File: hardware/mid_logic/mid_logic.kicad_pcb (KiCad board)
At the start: 4 copper layers, 52 x 52 mm, 49 parts, among them J2 J_STK_A, J3 J_STK_B, J7 USB-C, Q2 BC847, SW1 RESET, SW2 BOOT, U1 ESP32-S3-WROOM-1-N16R8, U2 MAX3485, U3 PCF8575, U4 PhotoMOS 60V, U5 USBLC6-2SC6

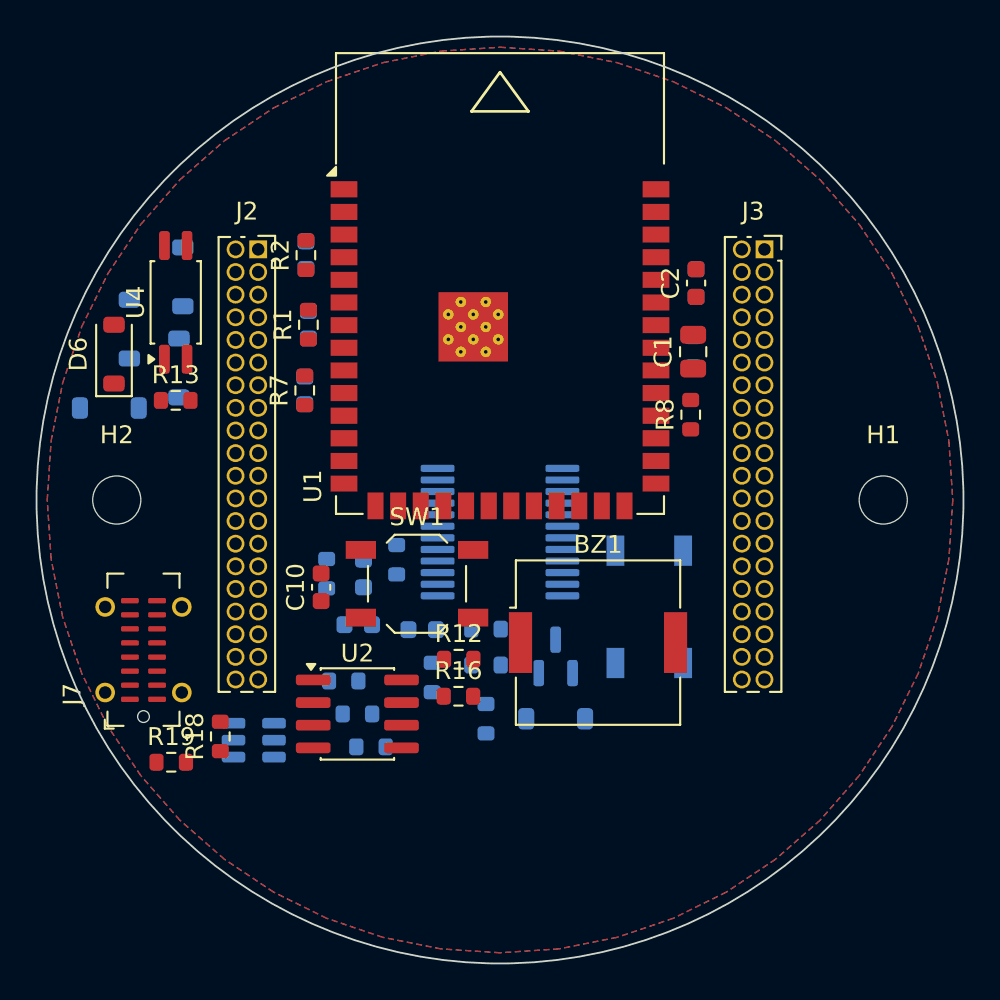
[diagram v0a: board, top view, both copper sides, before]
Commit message: Alle drei Boards kupferfehlerfrei, und die Bilder zeigen endlich die Stecker
ROUTING. Alle drei Platinen haben jetzt null Kupferfehler:

  Top     179 Segmente,  22 Vias,  7 Signale offen  (vorher 11, 2 Fehler)
  Mid     720 Segmente,  74 Vias,  4 Signale offen  (vorher  6)
  Bottom  811 Segmente,  91 Vias,  6 Signale offen  (vorher  8, 6 Fehler)

Top hatte zwei copper_edge_clearance-Fehler an der USB-C-Kerbe: Eine
BTN2-Bahn lief auf In1.Cu quer durch den Ausschnitt. Der Randkeepout des
Routers kannte die Kerbe gar nicht - er bestand aus vier Balken entlang der
Kanten, und die Kerbe schneidet in eine dieser Kanten hinein. Die einzige
Aussparung darin stammte noch von der Klinkenbuchse, die es nicht mehr gibt.
route_boards.py setzt jetzt NOTCH_KEEPOUT.

M1_ISNS AUF BOTTOM IST MIT ABSICHT LEER. Freerouting hatte das analoge
Motorstrom-Messsignal auf F.Cu direkt an die Vergleichsschwelle V_TRIP_LO
gepresst - vier Kurzschluesse, eine Kreuzung, ein Abstandsfehler, alle in
einem Feld von zwei Millimetern. Einzeln herausgeloeste Segmente haben das
Problem nur verschoben: nach jedem Eingriff dieselben zwei Netze an der
naechsten Stelle. Das Netz ist deshalb komplett entfernt und wird von Hand
gezogen. Sachlich ist die Paarung ohnehin die schlechteste denkbare - koppeln
Messsignal und Ausloeseschwelle, verstimmt sich die Hinderniserkennung
selbst, ohne dass eine DRC das je bemerkt. docs/16 erklaert es samt Auflagen.

DIE BILDER ZEIGTEN DIE STECKVERBINDER NICHT - und es lag nicht an den
Modellen. Die Bildkette war nie ein Skript, sondern jedes Mal von Hand
getippt. Dadurch stammten die Teile aus verschiedenen Zeitpunkten: Modelle
16:04, Stapel-STEPs 15:59, Unterseiten-Renderings 13:41. Ausgerechnet die
Unterseiten zeigen den Feldstecker und die USB-Buchse.

tools/render_all.py macht daraus einen Aufruf: sechs Boardansichten, drei
STEP-Ausgaben mit Modellen, das Stapelbild und die Gesamtbaugruppe - ein
Zeitstand fuer alles. Renderings jetzt mit transparentem Hintergrund, damit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
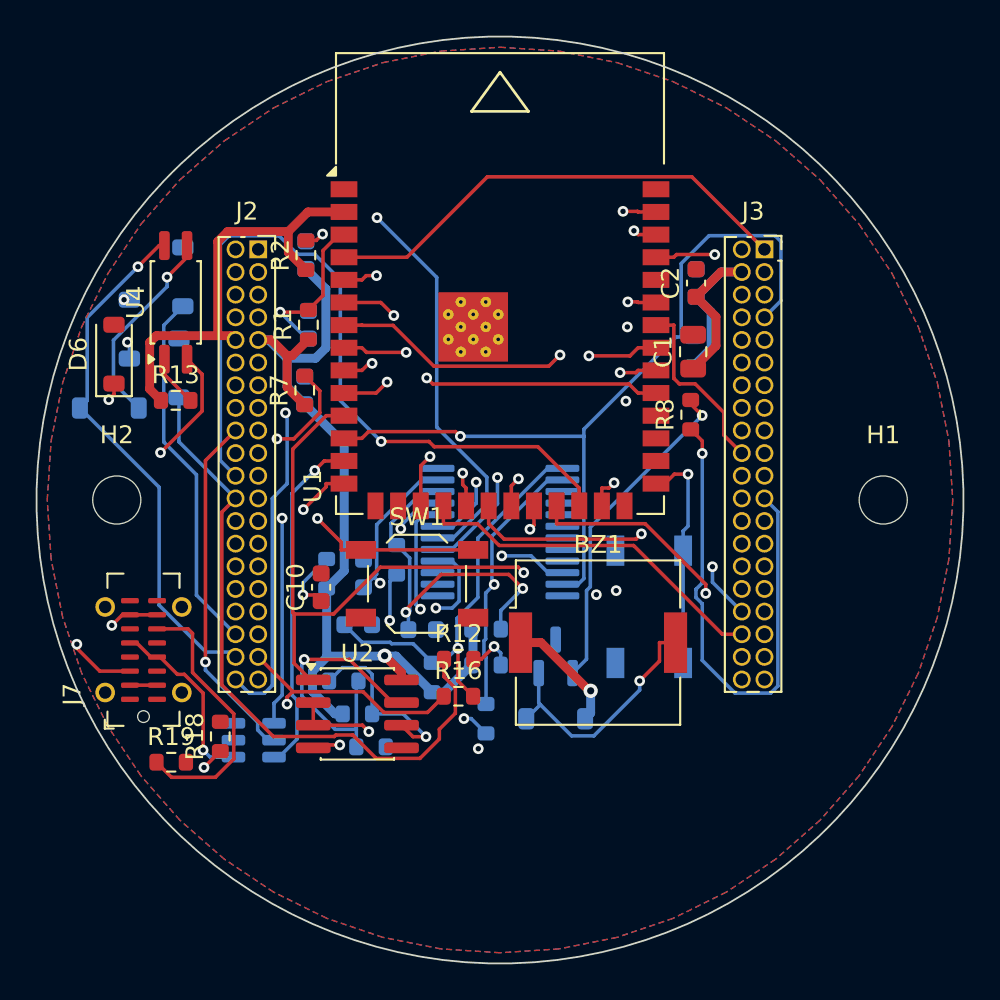
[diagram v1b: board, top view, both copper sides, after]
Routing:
- net 3V3_SYS: track 0.00 -> 124.0 mm, vias 0 -> 1
- net I2C_SCL: track 0.00 -> 61.6 mm, vias 0 -> 4
- net AUDIO_PWM: track 0.00 -> 56.9 mm, vias 0 -> 3
- net UART485_TX: track 0.00 -> 54.0 mm, vias 0 -> 2
- net TRIP_RST: track 0.00 -> 52.5 mm, vias 0 -> 1
- net SAB2_IN: track 0.00 -> 49.6 mm, vias 0 -> 2
- net HW_TRIP1: track 0.00 -> 49.0 mm, vias 0 -> 2
- net UART485_RX: track 0.00 -> 48.3 mm, vias 0 -> 1
- net I2C_SDA: track 0.00 -> 46.8 mm, vias 0 -> 1
- net I_SENSE2: track 0.00 -> 44.7 mm, vias 0 -> 1
- net M2_INB: track 0.00 -> 44.5 mm, vias 0 -> 1
- net SAB1_IN: track 0.00 -> 44.4 mm, vias 0 -> 2
- net PRESENCE_INT: track 0.00 -> 43.6 mm, vias 0 -> 1
- net 5V_SYS: track 0.00 -> 42.3 mm, vias 0 -> 1
- net RELAY_CTL: track 0.00 -> 42.0 mm, vias 0 -> 2
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
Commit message: Hauptschalter, Magnetkontakt im Rahmen, verschraubter Stapel - Umbau v0.7
VIER ENTSCHEIDUNGEN VOM 19.08.2026, alle umgesetzt:

1. HAUPTSCHALTER. Bisher stand nach dem Verschrauben von Bottom und Mid
sofort 24 V auf allem - ohne dass das Top-Board steckte. Jetzt laeuft der
Gate-Pulldown des Verpolschutz-FETs als SCHLEIFE durch den Stapel:
Q1-Gate -> R1 -> EN_LOOP (Stapelkontakt B2, war PGND; Pinout v0.7) -> SW5
auf Top -> PGND. Neuer 1-M-Pullup R1B haelt das Gate bei offener Schleife
definiert an der Source. Top-Board fehlt ODER SW5 aus -> Q1 sperrt, nichts
bekommt 24 V. Der Schalter traegt nur den Teilerstrom (~20 uA).
SW5 ist ein Copal CVS-01 (1,5 mm hoch, unter der Scheibe, durch eine
Oeffnung bedienbar). Er sitzt HOCHKANT bei (11,9/-19,4): Das Fenster
zwischen ToF-Courtyard (bis 8,245) und Ecktaster (ab 15,205) ist 6,96 mm
breit, der Schalter waagerecht 7,69 - drei Anlaeufe bei 12,5, 11,0 und 11,9
endeten in DRC-Ueberlappungen, erst das Ausmessen statt Schaetzens der
Courtyards zeigte, dass NUR gedreht Platz ist.

2. MAGNETKONTAKT IN DEN ABDECKRAHMEN, unten mittig - dort haelt auch das
vorhandene DCX-909 (Gewinde OD 8, im Rahmen ist Platz; Messpunkt F14: ist
der Rahmen dort hohl?). Das Magnetlangloch im Top-Board (Zwischenloesung
von einem Tag) ist wieder raus, mit ihm die 6,8-mm-Grenze, an der jedes
Kaufteil scheiterte. Neu: KABELKERBE 5 x 2 unten mittig, J6 dahinter
mittig auf der Rueckseite. Router-Keepout entsprechend getauscht.

3. LOETSCHEIBE hardware/stern_puck/ (OE 16, zweilagig, DRC null Fehler):
verbindet die Steckseite des DCX-909 mit den Litzen des Sterns. Litzen
durch Fesselbohrungen faedeln, umschlagen, loeten - die Zugentlastung ist
die Bohrung, nicht das Zinn. Drei eigene DRC-Runden gebraucht: 2,0er Pads
beruehren sich bei 1,85 Stiftabstand, die Minus-Bruecke lief durch das
Plus-Pad, die Fesselbohrungen brauchten seitliche Lage und OE 16 statt 14.

4. BEFESTIGUNGSKONZEPT v2 (docs/04, 2b): verschraubt statt nur gesteckt.
NEU mechanical/tragring.py 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
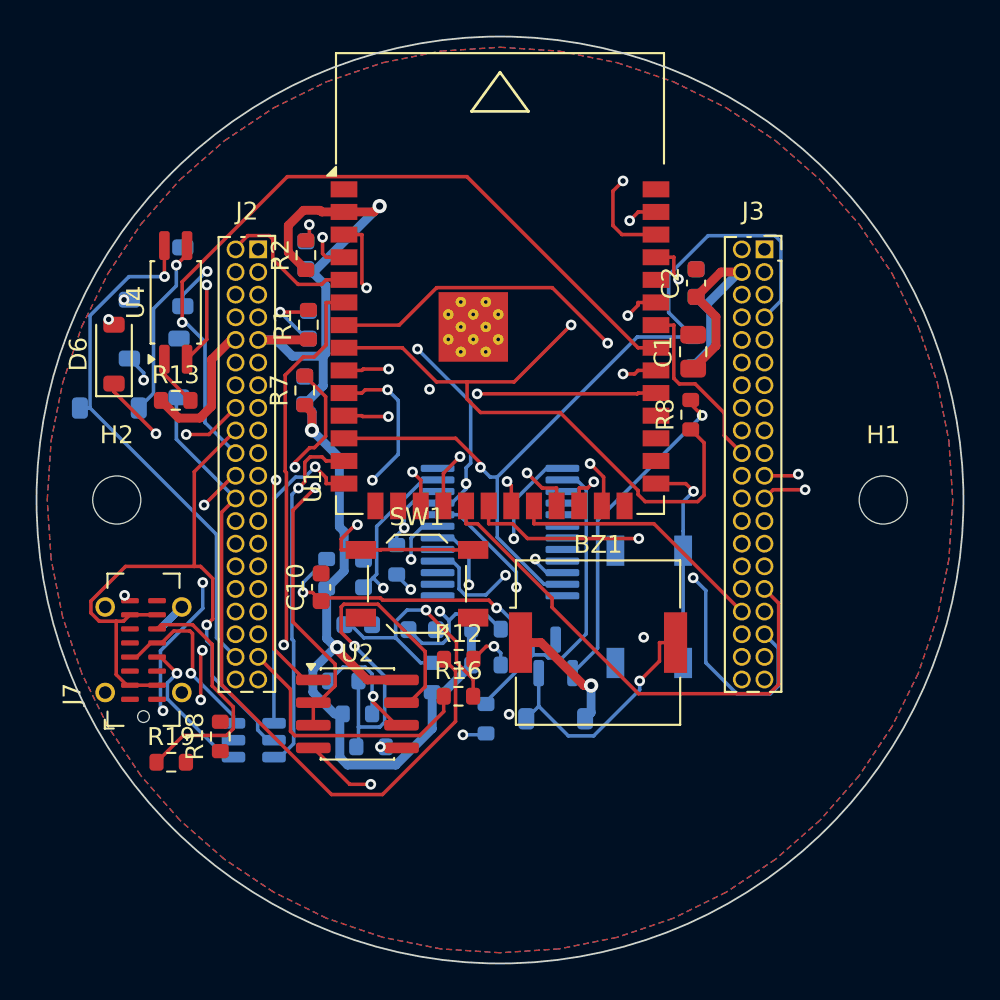
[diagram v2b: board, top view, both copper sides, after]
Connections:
- J3 pad 2: PGND -> EN_LOOP
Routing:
- net TRIP_RST: track 52.5 -> 29.1 mm
- net HW_TRIP2: track 21.9 -> 0.00 mm, vias 1 -> 0
- net USB_CC1: track 15.4 -> 0.00 mm, vias 2 -> 0
- net RS485_DIR: track 37.0 -> 49.6 mm
- net M2_INB: track 44.5 -> 54.9 mm, vias 1 -> 3
- net USB_DP_C: track 0.00 -> 10.2 mm, vias 0 -> 1
- net AUDIO_PWM: track 56.9 -> 66.9 mm, vias 3 -> 2
- net M1_INA: track 38.4 -> 47.8 mm, vias 1 -> 2
- net RS485_B: track 19.3 -> 28.1 mm
- net USB_VBUS: track 30.3 -> 37.7 mm, vias 2 -> 1
- net RELAY_CTL: track 42.0 -> 48.5 mm, vias 2 -> 3
- net PGND: track 0.00 -> 6.00 mm, vias 1 -> 4
- net I2C_SCL: track 61.6 -> 66.9 mm, vias 4 -> 3
- net HW_TRIP1: track 49.0 -> 43.9 mm, vias 2 -> 4
- net RS485_A: track 28.8 -> 23.8 mm, vias 1 -> 3
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
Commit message: Leistungsvias, Via-Strompruefung, Reset/Boot-Durchgriffe und der Gehaeusebecher
VIER ARBEITEN AUS EINEM ABEND, alle aus Rueckfragen entstanden:

1. VIAS SIND NICHT BELIEBIG STROMTRAGFAEHIG - der Einwand traf: 24V_IN
lief ueber genau EIN 0,6/0,3-Via (~1,2 A) bei 4,1 A Grenzstrom, dazu 14
weitere Engpaesse auf Bottom. Ursache: Die Bottom-Klassen routeten mit dem
Standardvia - ein Erbe der diskreten H-Bruecke, zwischen deren FETs das
0,8er nicht passte; Mid und Top hatten das Leistungsvia laengst. Jetzt:
PWR- und RAIL-Klasse auf Bottom mit 0,8/0,4, Massebruecken dort ebenso
(deren Platzsuche folgt jetzt der Viagroesse - die alte 0,6er-Suche setzte
0,8er-Vias in 0,6er-Luecken, vier Abstandsfehler).

NEU tools/via_check.py: prueft nach jedem Routing jedes Via gegen den
Dauerstrom seines Netzes (4 A je mm Bohrung, 3-mm-Parallelgruppen);
--fix setzt Zwillingsvias. Zwei eigene Fehler auf dem Weg, beide vom
Werkzeug selbst aufgedeckt: KiCad-10-Formabfragen brauchen eine Lage, und
die erste Freiraumpruefung sah nur F/B - ein Via bohrt aber durch ALLE
vier Lagen; 15 Innenlagen-Kurzschluesse, alle rueckstandslos entfernt.
Endstand: 27 Zwillinge gesetzt, 11 dokumentierte Engpaesse als
Handarbeitsliste mit Koordinaten in docs/16.

2. RESET UND BOOT WAREN UNERREICHBAR - SW1 sass mitten unter dem
Top-Board, SW2 zeigte zur Rueckseite. Beide jetzt auf Mids Vorderseite bei
(+-8/18,6), darueber zwei OE-3,2-Durchgriffe H3/H4 im Top-Board: Scheibe
ab, Stift durch, druecken. Im Betrieb verdeckt die Scheibe die Loecher.

3. DER GEHAEUSEBECHER (mechanical/gehaeuse.py): kapselt Bottom und Mid,
Rueckwand mit Tunnelfenster fuer die Feldstecker-Leiste - sie bleibt als
einziges von hinten zugaenglich. Verbindung zum Tragring per BAJONETT:
drei Zapfen an 12/3/9 Uhr, ~7 Grad Drehung, tangential auskragende
Koepfe - radiale Rasthaken scheiterten dreifach (Adapter auf den
Diagonalen, Dosenwand aussen, Adapterbasis innen; frei ist nur ein
2,2-mm-Band auf den Achsen). Wand an den Schraubdomen gefenste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
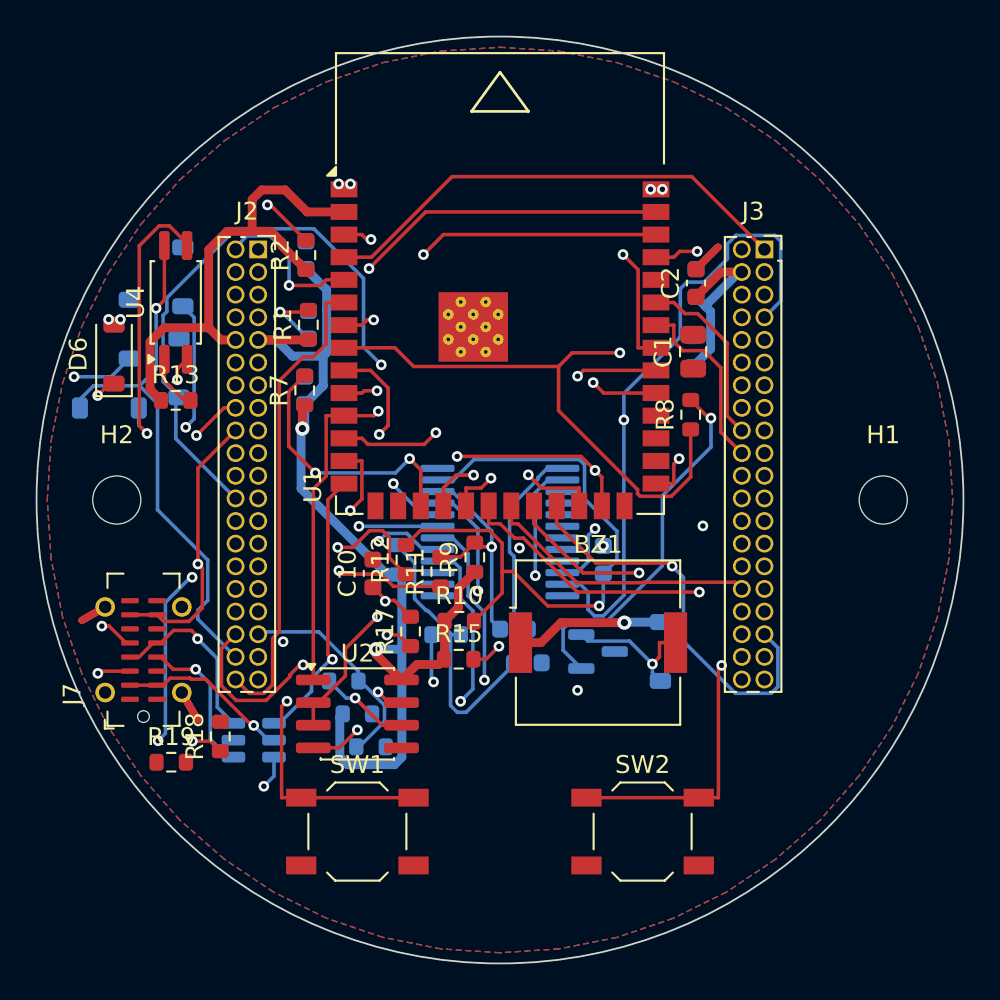
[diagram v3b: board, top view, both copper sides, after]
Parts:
- R10, R11, R15, R17, R9, SW2: moved to F.Cu
- R16: moved to B.Cu
- moved SW1 14.3 mm to (-8.00, 18.6)
- moved C8 13.5 mm to (5.80, 3.35)
- moved SW2 12.6 mm to (8.00, 18.6), turned to 0 degrees
- moved C9 9.75 mm to (1.56, 9.14)
- moved R15 8.82 mm to (-2.32, 8.93), turned to 0 degrees
- moved D1 6.98 mm to (9.00, 8.50), turned to 90 degrees
- moved R14 6.90 mm to (-5.80, 3.35)
- moved R17 6.47 mm to (-5.02, 7.37)
- moved R12 6.32 mm to (-5.28, 3.35), turned to 90 degrees
- moved C7 5.15 mm to (0.78, 7.24)
- moved R9 4.08 mm to (-1.41, 3.21), turned to 90 degrees
- moved R16 3.52 mm to (-3.02, 7.56)
- moved C10 3.00 mm to (-7.13, 4.12)
- moved R10 2.88 mm to (-2.28, 6.80)
- moved R11 2.56 mm to (-3.33, 4.02)
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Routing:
- net ESP_BOOT: track 43.1 -> 62.3 mm
- net SAB1_IN: track 41.6 -> 59.3 mm, vias 1 -> 2
- net EXP_P7: track 19.3 -> 35.2 mm, vias 2 -> 1
- net PGND: track 6.00 -> 20.0 mm, vias 4 -> 7
- net RS485_B: track 28.1 -> 14.1 mm
- net USB_CC2: track 14.0 -> 0.00 mm
- net M2_INB: track 54.9 -> 41.0 mm, vias 3 -> 1
- net TRIP_RST: track 29.1 -> 42.9 mm, vias 1 -> 3
- net HW_TRIP2: track 0.00 -> 11.9 mm, vias 0 -> 1
- net EXP_P9: track 34.5 -> 23.3 mm, vias 2 -> 3
- net ESP_EN: track 36.3 -> 47.4 mm
- net USB_CC1: track 0.00 -> 10.5 mm, vias 0 -> 2
- net REED2_IN: track 39.0 -> 49.4 mm, vias 0 -> 2
- net UART485_TX: track 56.7 -> 46.4 mm, vias 3 -> 2
- net RS485_DIR: track 49.6 -> 39.9 mm, vias 2 -> 3
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
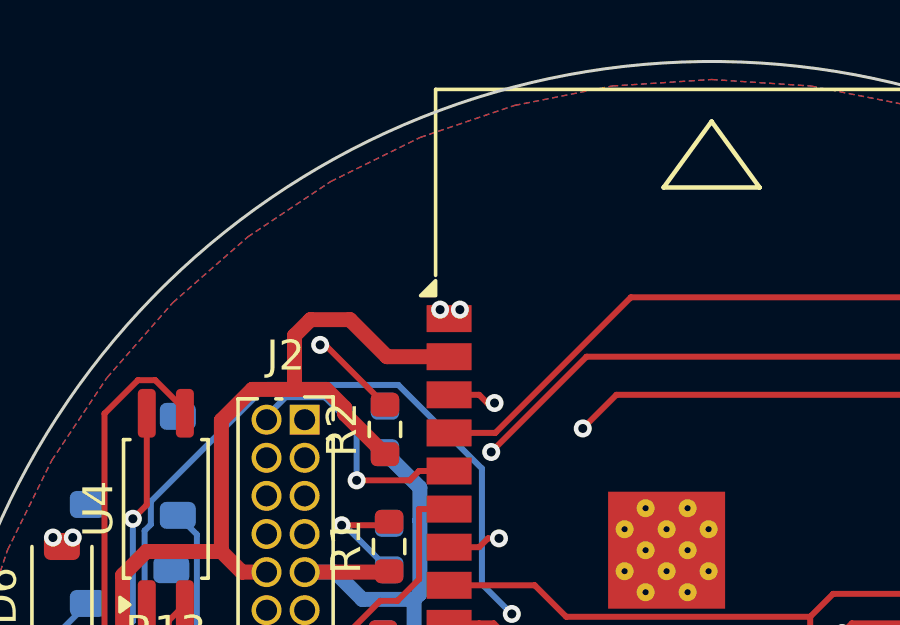
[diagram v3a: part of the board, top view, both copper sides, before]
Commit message: Bestellfaehigkeit Punkt fuer Punkt - und das Flip-Flop war unbestueckbar
Die Frage "was ist entscheidend fuer Fertigung und Bestueckung?" wurde als
Sieben-Punkte-Liste beantwortet und abgearbeitet:

1. NETZE: Zweiter Freerouting-Pass ueber alle drei Boards - die neue
Erkenntnis (Altbahnen gelten als Vorverdrahtung) als Werkzeug genutzt.
Mid faellt auf 3 offene Signale. Top ist geometrisch festgefahren (9),
Bottom nach Neuerzeugung bei seinen Restnetzen - alles dokumentierte
Handarbeit in docs/16. gen_fab bleibt bis dahin zu Recht verriegelt.

2. KUPFER: Alle drei Boards null Fehler. Drei Nacharbeiten auf dem Weg:
ein Brueckenvia 0,33 mm vor der Bottom-Kante nach innen gerueckt, das
RELAY_CTL-Segment an der USB-Bohrung erneut entfernt (Freerouting legt es
in dieselbe Luecke - ein Keepout scheidet aus, weil die USB-Pads nur
1,0 mm neben den Loechern liegen; bleibt Handarbeit), und die
LCSC-Felder unsichtbar gestellt, die als sieben ungespiegelte C-Nummern
im Bestueckungsdruck der Rueckseite auftauchten.

3. LCSC: 13 Nummern verifiziert (jede von einer LCSC-Produktseite,
nichts geraten) und doppelt verdrahtet - in den Schaltplan-Generatoren
fuer kuenftige Neuerzeugungen, per neuem tools/lcsc_nachtragen.py auf
den fertig gerouteten Boards. Fehlend: 262 statt 302. Ehrlich offen:
TLV3702 (LCSC fuehrt nur die TLC-Variante, die am Gleichtaktbereich
scheitert), VL53L1X, Micro-Fit 43045-1612 (THT, zur Not von Hand).

DER WICHTIGSTE FUND STECKTE IM LCSC-ABGLEICH: Das Trip-Latch 74AUP1G74
stand im 5-Pin-SOT-353 - ein D-Flip-Flop hat ACHT Pins, 6/7/8 hingen in
der Luft. Jedes gefertigte Bottom waere Schrott gewesen. Jetzt VSSOP-8
(SN74AUP1G74DCUR, C140267), Bottom komplett neu erzeugt und geroutet -
974 Segmente, 121 Vias, mit SENSE-Abstandsklasse (300 um) fuer
M1_ISNS/M2_ISNS gegen die Trip-Schwellen.

4. NUTZEN: kupferfehlerfrei; die zwoelf verbleibenden DRC-Meldungen sind
EINE Sache (Mausbiss-Bohrungen des 12-Uhr-Stegs in der grosszuegigen
ESP32-Sperrflaeche - kein Kupfer, en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
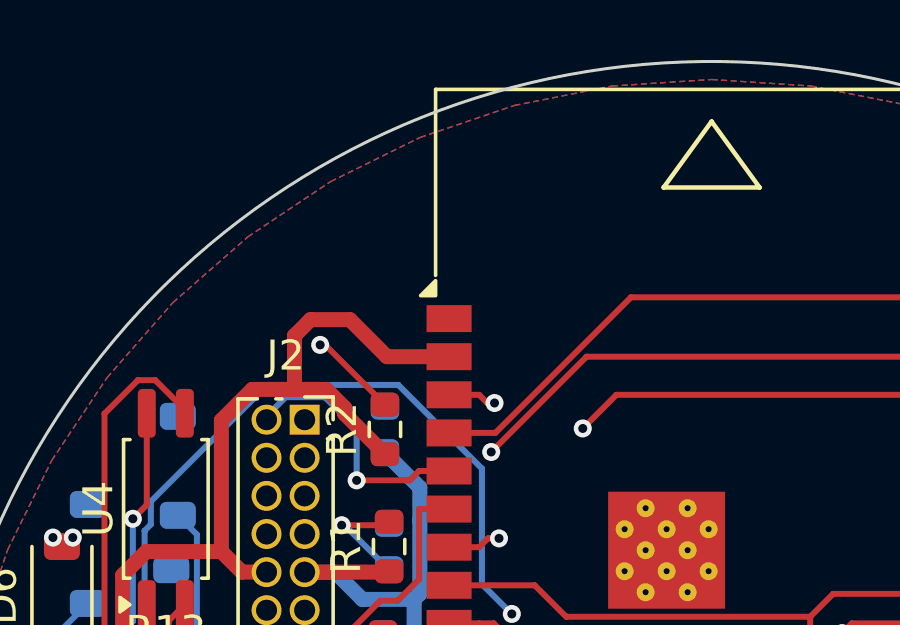
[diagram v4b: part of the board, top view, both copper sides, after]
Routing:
- net PGND: vias 7 -> 5

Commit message: Explosionszeichnung erzaehlt die Einbaureihenfolge - Feldstecker zuerst
Schnitt A ist auf Wunsch in die echte Montagefolge umsortiert:
Feldstecker (neu gezeichnet - er fehlte schlicht) -> Bottom -> Mid ->
Tragring -> Abdeckrahmen -> Scheibenadapter -> Top-Board (mit Panel und
Schaum) -> Zentralscheibe zuletzt, kraftfrei aufgeklickt. Der Untertitel
sagt es jetzt woertlich: Reihenfolge = Einbaureihenfolge.

Die eng zusammengerueckte Mittelgruppe brauchte vier Anlaeufe
Beschriftungsstaffelung (Tragring/Adapter/Rahmen in drei Baendern,
Texte gekuerzt, Schaumfahne hoeher) - per Bildausschnitt geprueft.

Co-Authored-By: Claude Opus 5 <noreply@anthropic.com>
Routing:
- net PGND: track 20.0 -> 0.00 mm, vias 5 -> 0
- net RELAY_CTL: track 46.3 -> 50.2 mm
